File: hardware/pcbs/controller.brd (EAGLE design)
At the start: 40 x 16 mm, 47 parts, among them U1 ATMEGA328

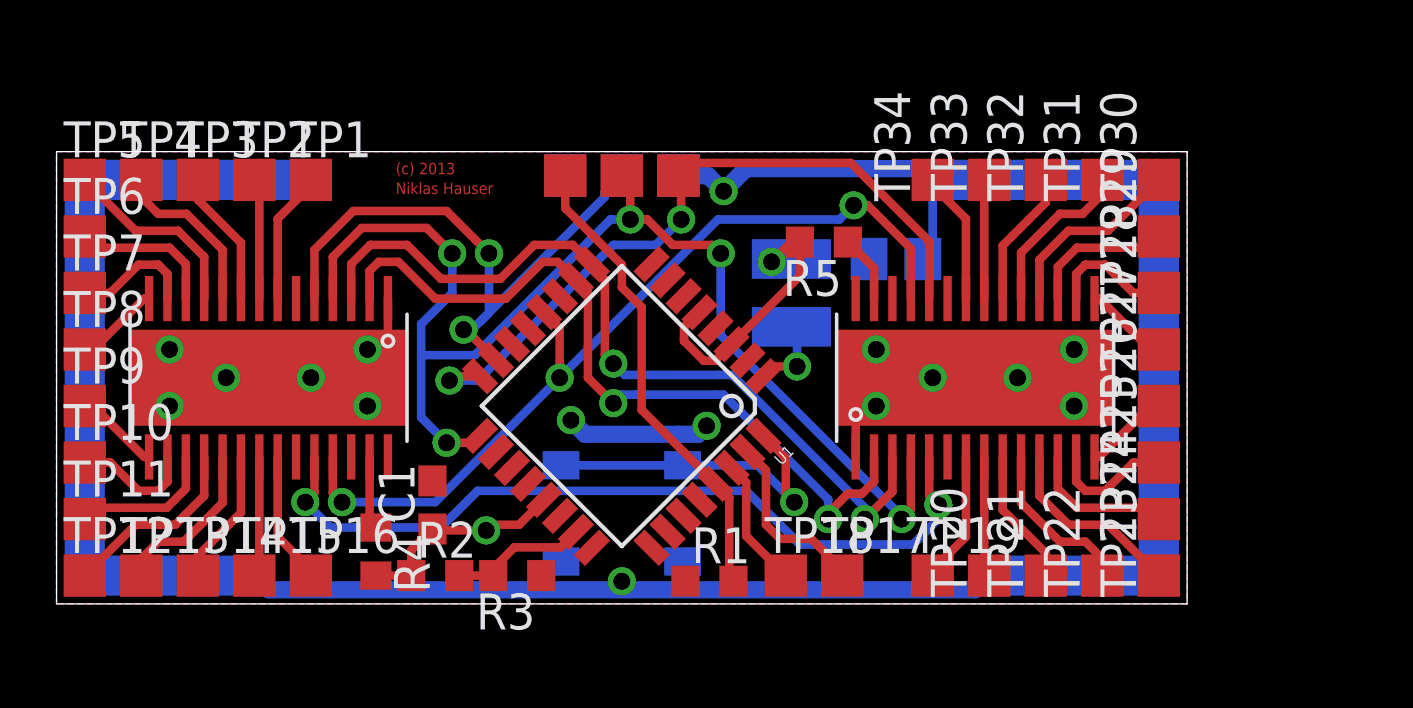
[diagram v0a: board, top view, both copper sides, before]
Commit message: Remove first two pcb iterations and replace with the third working one.
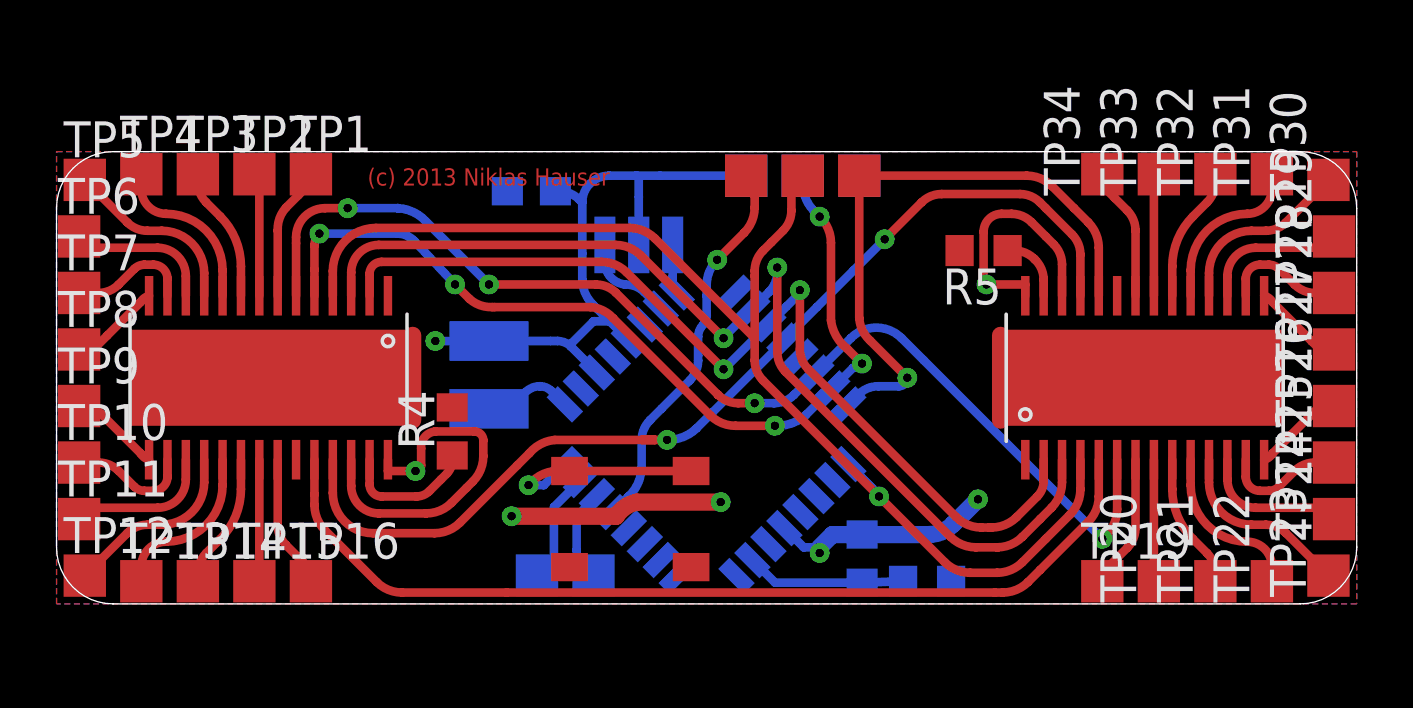
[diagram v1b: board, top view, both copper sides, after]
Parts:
- removed C2: (no value), rcl:C0805
- removed R1: 1k, rcl:R0603
- added U$5: CSRCE8, bookla:CSTCE_G
- C1: value (none) -> 100nF
- R2, R3: value 1k -> 10k
- U$6: device bookla:EVQPSD -> bookla:EVQPSG02K
- moved R2 15.1 mm to (28.5, 1.60), flipped to the bottom, turned to 270 degrees
- moved R3 14.5 mm to (30.8, 0.80), flipped to the bottom, turned to 0 degrees
- moved C1 11.6 mm to (16.8, 14.6), flipped to the bottom, turned to 0 degrees
- moved U$4 11.1 mm to (15.3, 8.10)
- moved TP17 10.8 mm to (17.0, 1.00), flipped to the bottom
- moved TP18 6.80 mm to (19.0, 1.00), flipped to the bottom
- moved U$2 6.40 mm to (26.4, 16.0)
- moved TP24 6.20 mm to (45.2, 3.00)
- moved TP25 6.20 mm to (45.2, 5.00)
- moved TP26 6.20 mm to (45.2, 7.00)
- moved TP27 6.20 mm to (45.2, 9.00)
- moved TP28 6.20 mm to (45.2, 11.0)
- moved TP29 6.20 mm to (45.2, 13.0)
- moved TP19 6.00 mm to (37.0, 0.80)
- moved TP20 6.00 mm to (39.0, 0.80)
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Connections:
- net N$4 renamed RX
- new net VPRG: U$1.P6, U$3.P6, U1.14
- new net XLAT1: U$5.1, U1.7
- new net XLAT2: U$5.3, U1.8
- net BLANK: now also U1.11; no longer U1.10
- net GND: now also U$5.2; no longer C2.1
- net RESET: no longer R1.2
- net VCC: now also U$1.P26, U$3.P26; no longer C2.2, R1.1
- net XLAT: now also U1.10; no longer U1.9
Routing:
- net VCC: track 100.4 -> 28.6 mm
- net VPRG: track 0.00 -> 40.5 mm, vias 0 -> 4
- net MOSI: track 21.2 -> 32.1 mm, vias 2 -> 5
- net GND: track 28.3 -> 37.1 mm, vias 14 -> 3
- net XLAT: track 29.1 -> 36.9 mm
- net BLANK: track 27.8 -> 33.8 mm
- net GSCLK: track 31.2 -> 36.3 mm, vias 3 -> 2
- net SOUT: track 28.5 -> 33.6 mm, vias 2 -> 0
- net BUTTON: track 11.6 -> 7.47 mm
- net MISO: track 25.6 -> 21.6 mm, vias 2 -> 1
- net RESET: track 17.1 -> 13.6 mm, vias 0 -> 1
- net XLAT1: track 0.00 -> 3.21 mm
- net TX: track 6.41 -> 4.08 mm
- net N$8: track 2.56 -> 4.76 mm
- net XLAT2: track 0.00 -> 1.71 mm
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- added copper zone on layer 1, net GND
- added copper zone on layer 16, net VCC
- removed copper zone on layer 16, net GND
- removed copper zone on layer 1, net VCC
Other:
- board size 40 x 16 mm -> 46 x 16 mm
- board text added: "(c) 2013 Niklas Hauser"
- board text removed: "(c) 2013"
- board text removed: "Niklas Hauser"
